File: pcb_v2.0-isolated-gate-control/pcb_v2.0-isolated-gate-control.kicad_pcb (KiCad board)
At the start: 4 copper layers, 170 x 110 mm, 194 parts, among them J1 ServoLock, J10 Buttons, J11 2x encoder, J12 limit-g2, J13 Relay VFD2 [NO, COM, NC], J14 GND-P, J15 OD, J16 Power-LightBarrier-12V, J17 3V3 5V VDD, J18 GNDD, J19 OD, J2 supply, J20 OD, J21 limit-g1, J3 12V 5V, J4 light-barrier, reserve, J5 GND-P, J6 2x remoteControl, J7 Relay VFD1 [NO, COM, NC], J8 RS485, J9 Conn_01x03_Pin, K1 RT314A24, K2 RT314A24, Q1 2N7000, Q2 2N7000, Q3 IRF5305, Q6 IRF5305, U1 ULN2003, U2 esp32-devkit-v1_30Pin, U3 74HC04, U4 MAX485E, U5 L78S05CV_TO220

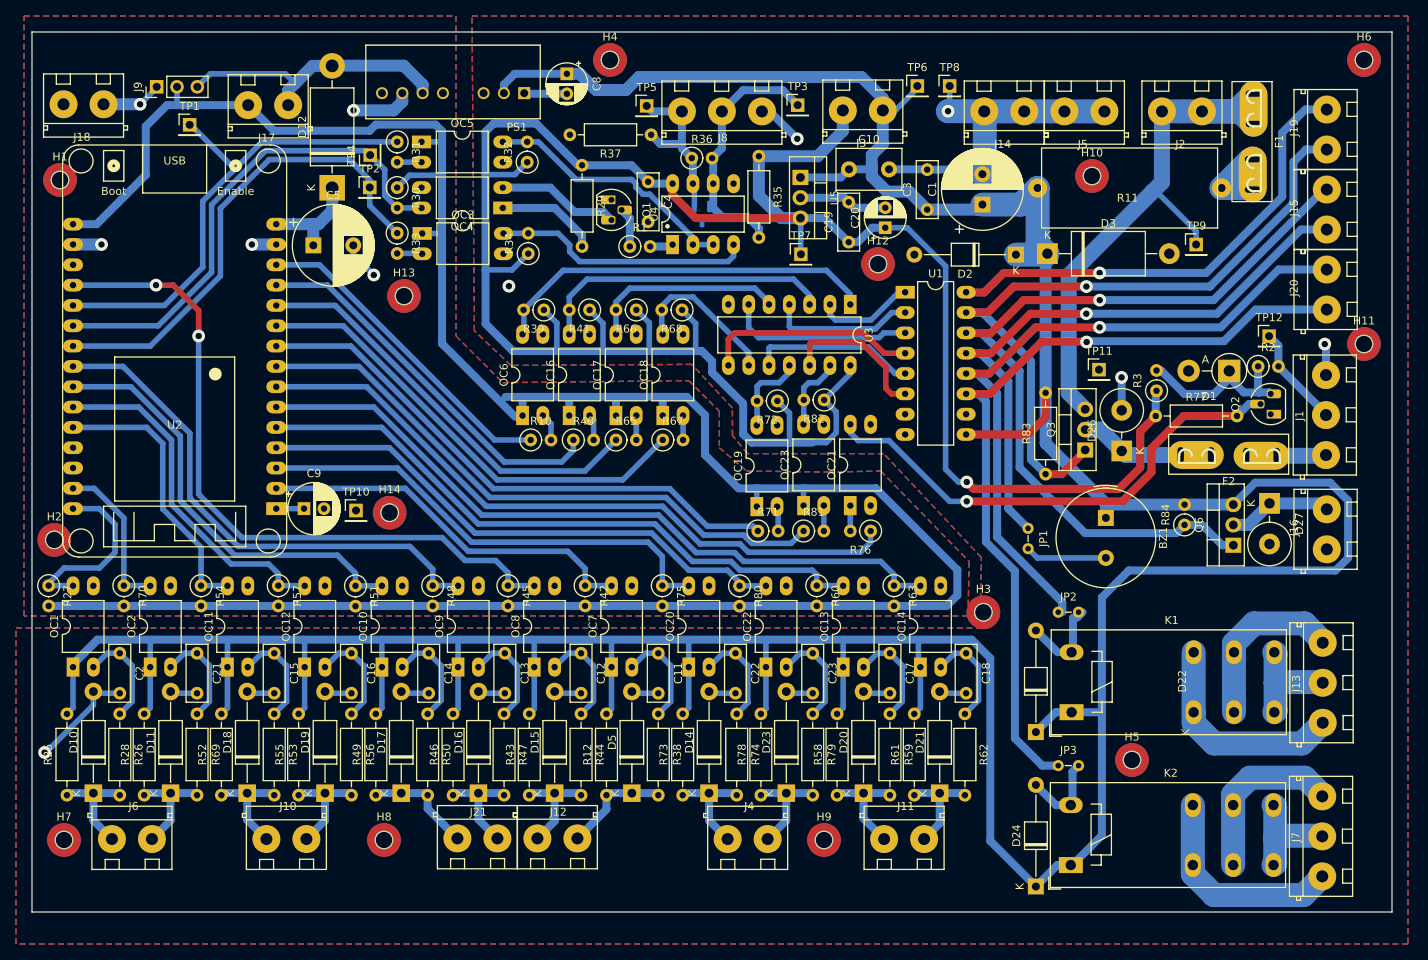
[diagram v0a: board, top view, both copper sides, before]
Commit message: pcb: Invert optocoupler-GPIO connection (high=output on), Layout adjusted (DRC pass)
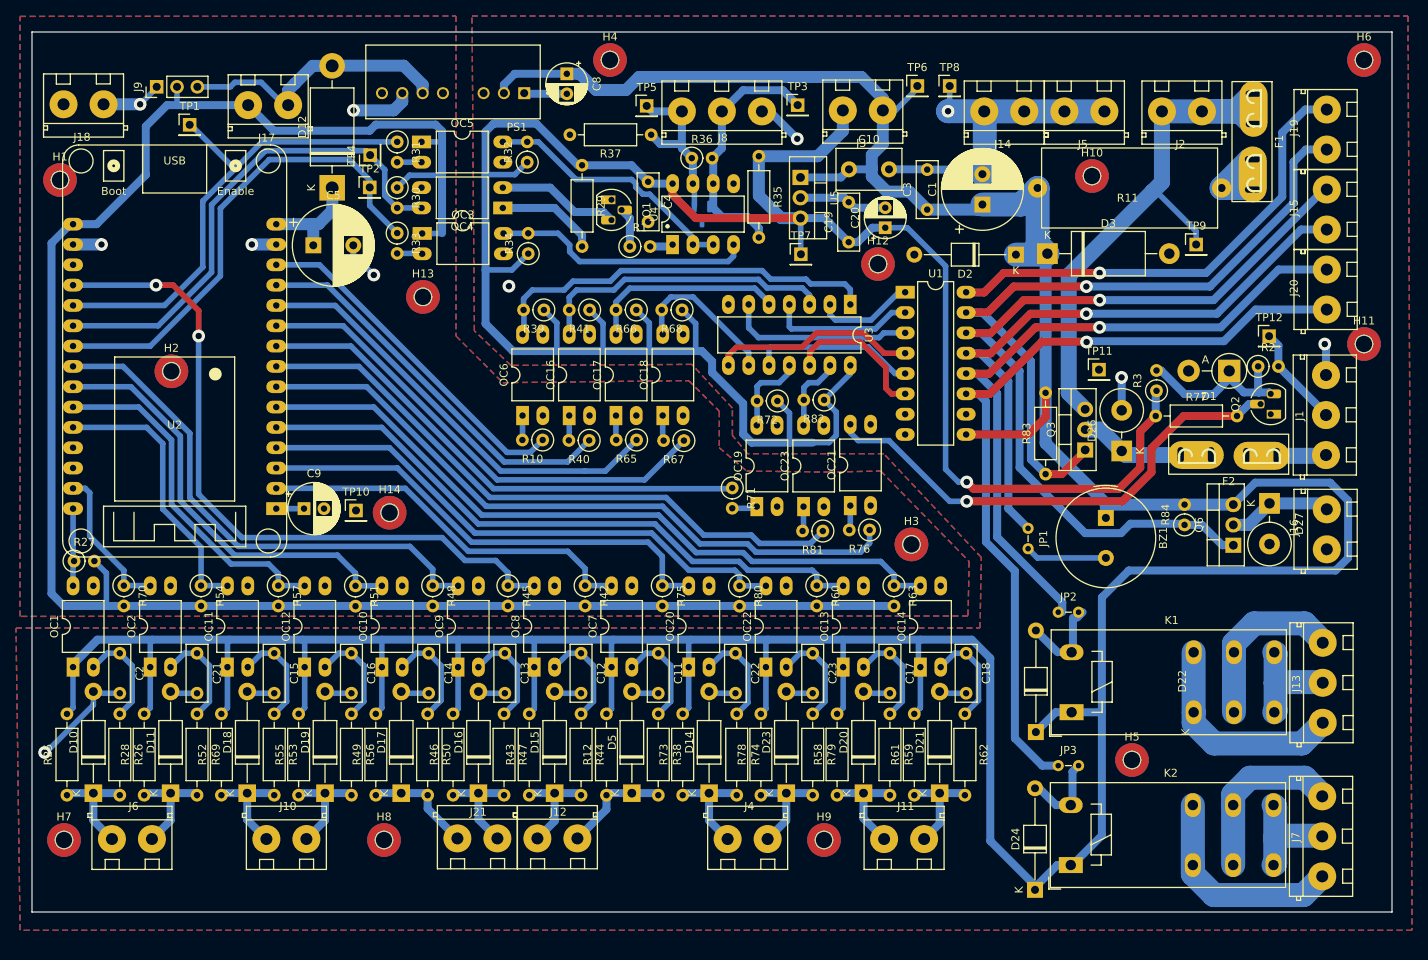
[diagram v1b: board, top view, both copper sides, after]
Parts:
- J4: value light-barrier, reserve -> light-barrier, switch
- R39, R41, R66, R68, R72: value 4k7 -> 6k8
- R82: value 10k -> 6k8
- moved H2 25.7 mm to (52.4, 67.4)
- moved H3 12.4 mm to (144.9, 89.1)
- moved R71 6.26 mm to (122.5, 82.0), turned to -90 degrees
- moved R27 4.41 mm to (40.3, 91.1), turned to 0 degrees
- moved R67 2.65 mm to (116.5, 76.1), turned to 180 degrees
- moved R65 2.57 mm to (110.6, 76.0), turned to 180 degrees
- moved R81 2.41 mm to (133.9, 87.4), turned to 180 degrees
- moved H13 2.37 mm to (83.9, 58.1)
- moved R40 1.98 mm to (104.6, 76.0), turned to 180 degrees
- moved R10 1.50 mm to (98.8, 76.0), turned to 180 degrees
- moved D24 0.43 mm to (160.4, 132.2)
- moved R76 0.18 mm to (139.7, 87.2)
- moved OC23 0.13 mm to (131.4, 84.3)
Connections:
- net /dIn_Reserve renamed /dIn_Switch
- OC16 pad 1: +3V3 -> Net-(OC16-Pad1)
- OC16 pad 2: Net-(OC16-Pad2) -> GND
- OC17 pad 1: +3V3 -> Net-(OC17-Pad1)
- OC17 pad 2: Net-(OC17-Pad2) -> GND
- OC18 pad 1: +3V3 -> Net-(OC18-Pad1)
- OC18 pad 2: Net-(OC18-Pad2) -> GND
- OC19 pad 1: +3V3 -> Net-(OC19-Pad1)
- OC19 pad 2: Net-(OC19-Pad2) -> GND
- OC23 pad 1: +3V3 -> Net-(OC23-Pad1)
- OC23 pad 2: Net-(OC23-Pad2) -> GND
- OC6 pad 1: +3V3 -> Net-(OC6-Pad1)
- OC6 pad 2: Net-(OC6-Pad2) -> GND
- R10 pad 2: Net-(OC6-Pad2) -> Net-(OC6-Pad1)
- R40 pad 2: Net-(OC16-Pad2) -> Net-(OC16-Pad1)
- R65 pad 2: Net-(OC17-Pad2) -> Net-(OC17-Pad1)
- R67 pad 2: Net-(OC18-Pad2) -> Net-(OC18-Pad1)
- R71 pad 2: Net-(OC19-Pad2) -> Net-(OC19-Pad1)
- R81 pad 2: Net-(OC23-Pad2) -> Net-(OC23-Pad1)
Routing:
- net +3V3: track 311.5 -> 244.0 mm
- net /dIn_RemoteOpen: track 22.8 -> 9.79 mm
- net /dOut_RelayEnVFD2: track 69.7 -> 64.4 mm
- net Net-(OC6-Pad2): track 3.47 -> 0.00 mm
- net Net-(OC16-Pad2): track 3.27 -> 0.00 mm
- net Net-(OC23-Pad2): track 3.18 -> 0.00 mm
- net Net-(OC18-Pad1): track 0.00 -> 3.17 mm
- net Net-(OC19-Pad1): track 0.00 -> 3.15 mm
- net Net-(OC16-Pad1): track 0.00 -> 3.12 mm
- net Net-(OC19-Pad2): track 3.11 -> 0.00 mm
- net Net-(OC23-Pad1): track 0.00 -> 3.10 mm
- net Net-(OC17-Pad1): track 0.00 -> 3.07 mm
- net Net-(OC6-Pad1): track 0.00 -> 3.06 mm
- net Net-(OC18-Pad2): track 3.06 -> 0.00 mm
- net Net-(OC17-Pad2): track 3.06 -> 0.00 mm
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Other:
- board text added: "12x digital-in Switch to GND non-inverting"
- board text added: "Gate V2.0 28.12.2024 pcb_isolated-gate-control"
- board text added: "LightBarrier Switch"
- board text added: "pullups to 12V"
- board text removed: "<="
- board text removed: "Digital Inputs"
- board text removed: "LightBarrier RESERVE"
- board text removed: "Switch to GND non-inverting"
- board text removed: "pcb_isolated-gate-control Gate V2.0 28.12.2024"

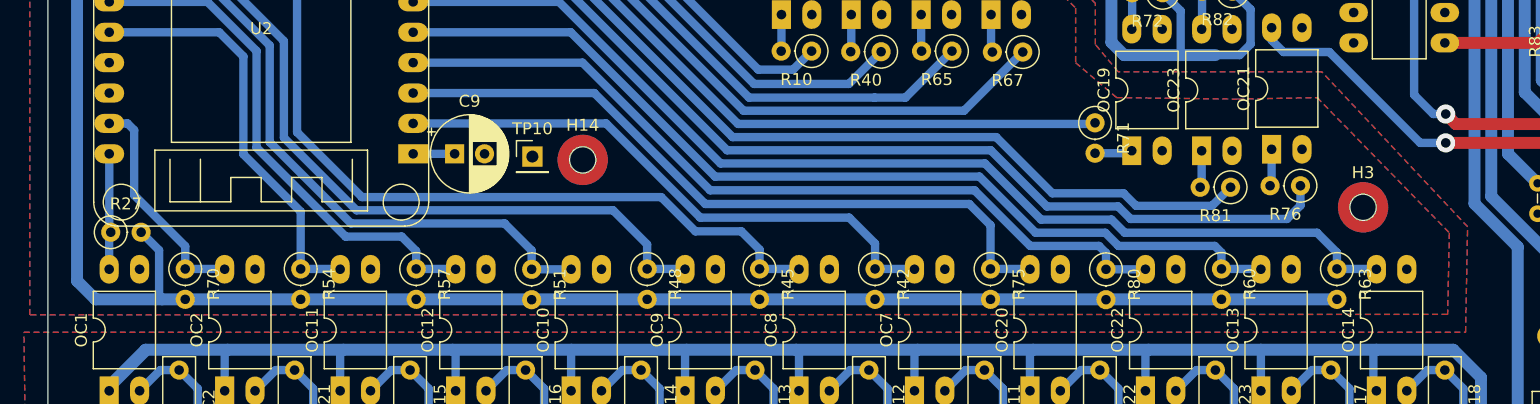
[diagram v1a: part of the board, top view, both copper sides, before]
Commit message: pcb: Cleanup Schematic, arrange, replace legacy-symbols, optimize for ERC pass
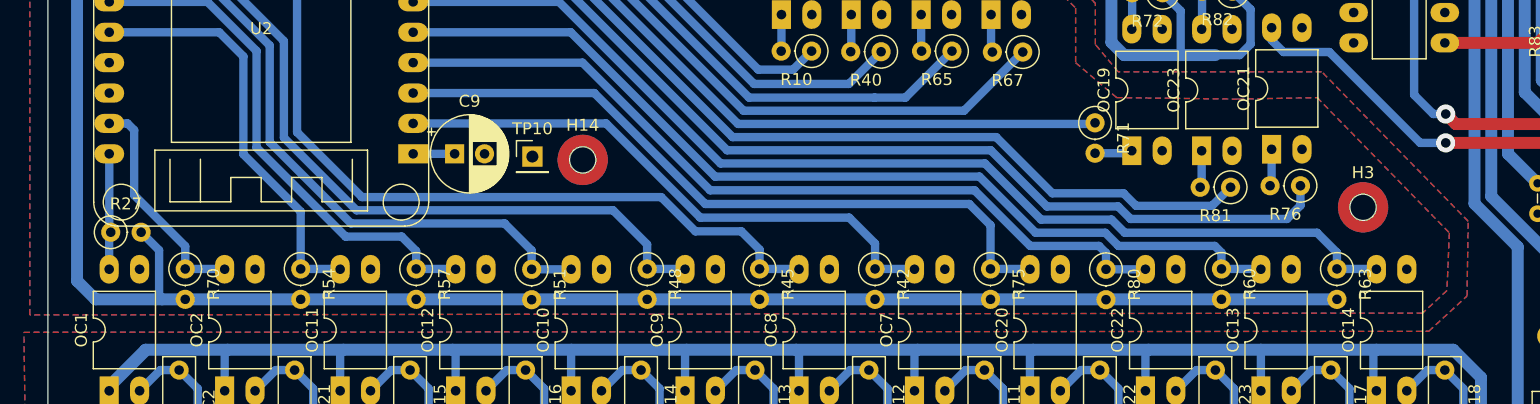
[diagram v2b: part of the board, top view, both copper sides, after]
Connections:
- net RS485_A renamed /RS485-A
- net RS485_B renamed /RS485-B

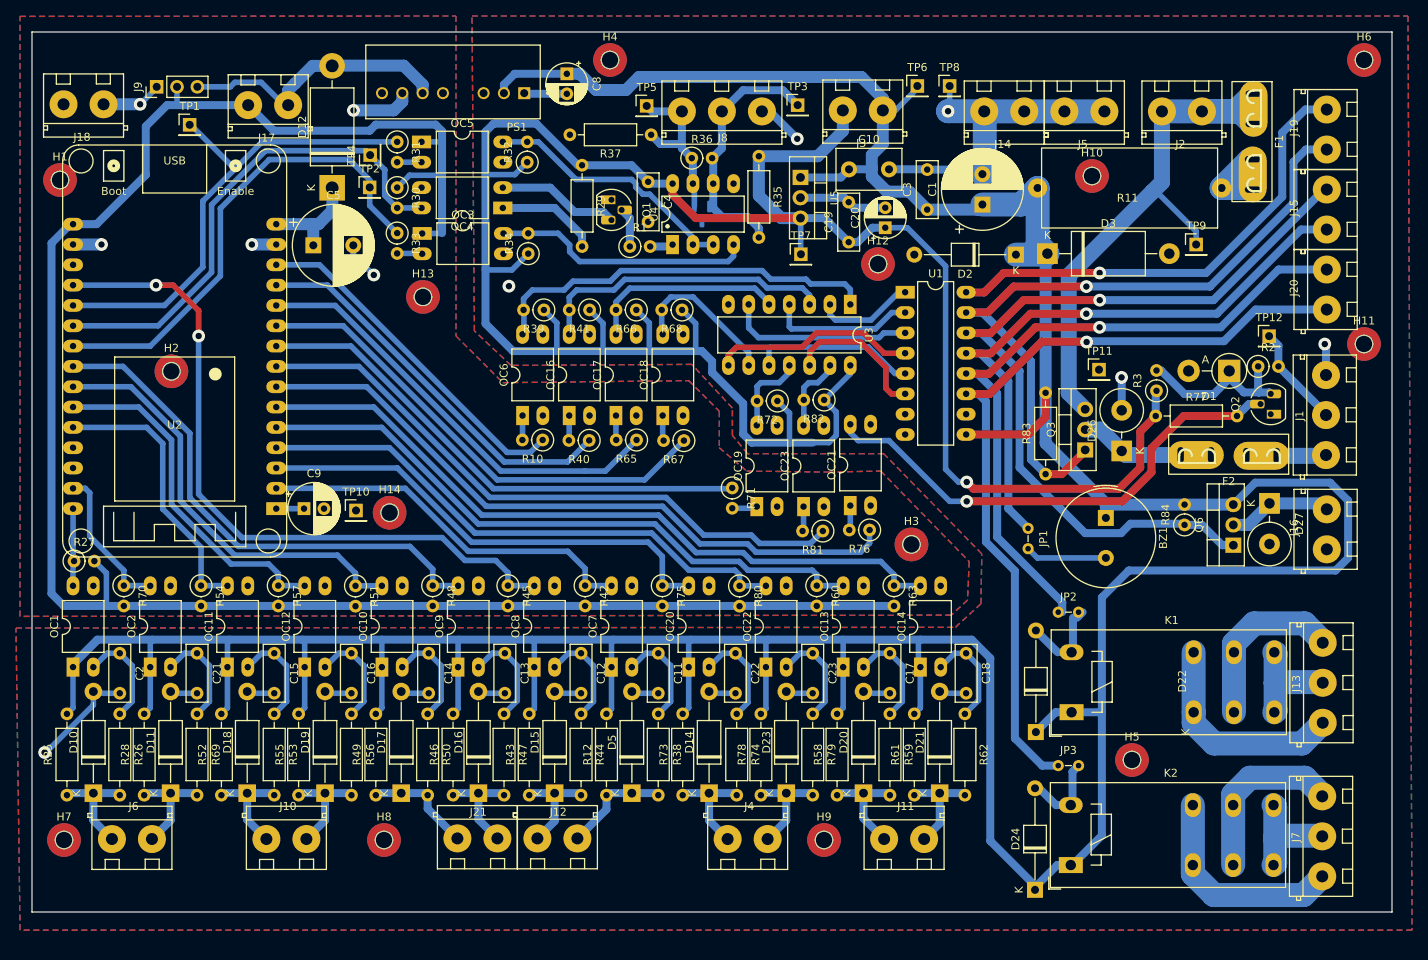
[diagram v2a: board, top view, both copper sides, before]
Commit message: pcb: finish todos, Fix esp32 power issues, document tests, dualType C footprint
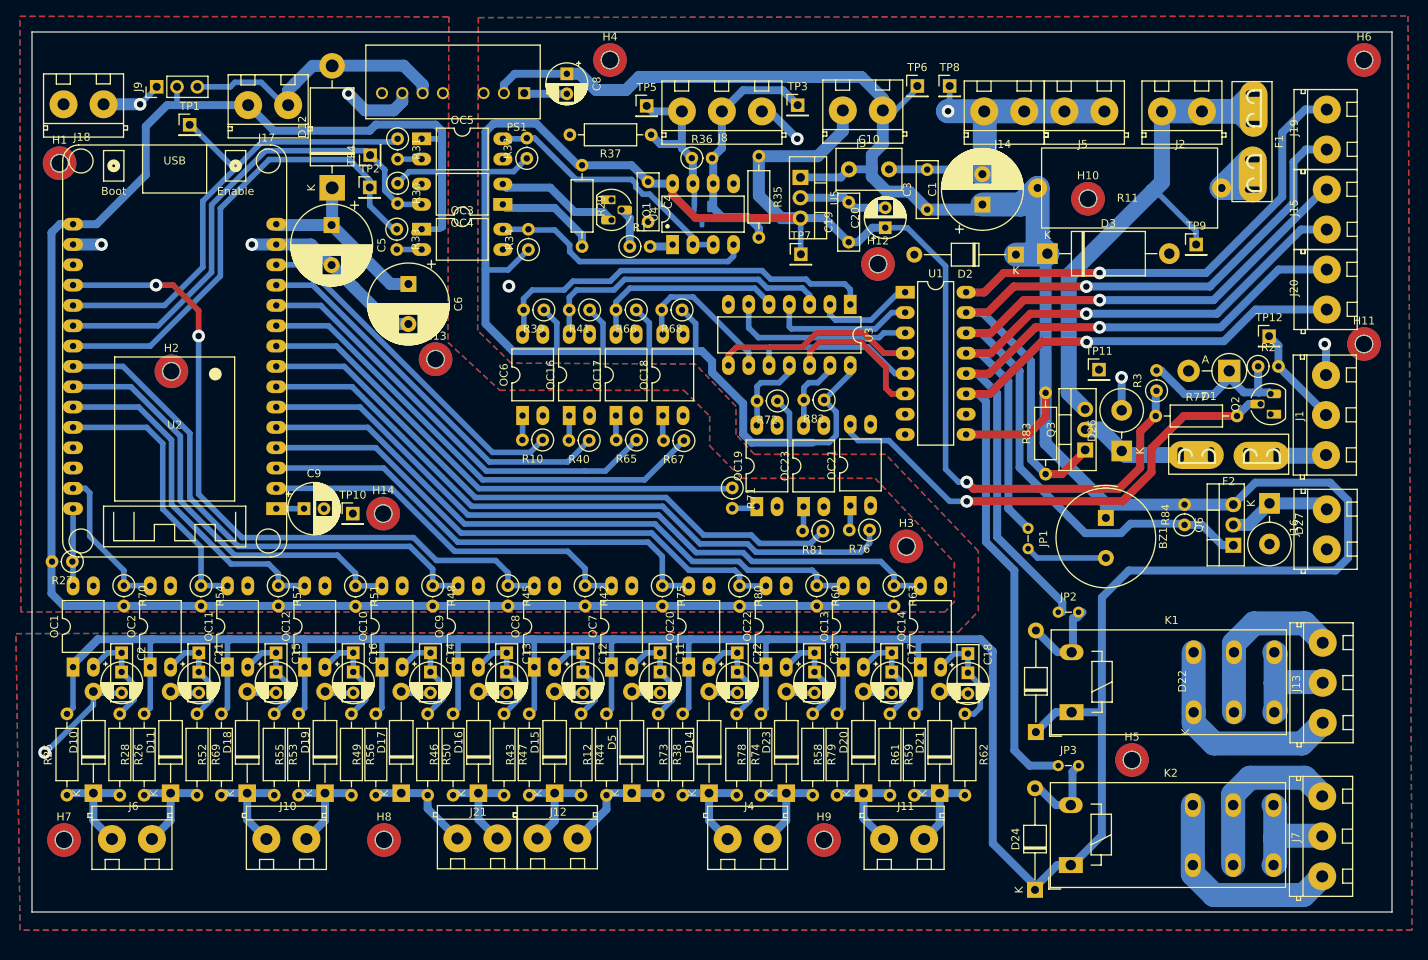
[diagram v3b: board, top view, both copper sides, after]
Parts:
- added C6: 2200uF, Capacitor_THT:CP_Radial_D10.0mm_P5.00mm, F.Cu at (82.0, 56.5)
- C11, C12, C13, C14, C15, C16, C17, C18, C2, C21, C22, C23: footprint Capacitor_THT:C_Disc_D7.0mm_W2.5mm_P5.00mm -> capacitor_libJonny:C_DualType__Disc-7.0x2.5mm-P5mm__Elko-D5mm-P2.5mm
- C5: value 330uF -> 2200uF
- R31, R33: value 470 -> 330
- moved H13 7.94 mm to (85.5, 65.9)
- moved C5 3.41 mm to (72.5, 49.1), turned to -90 degrees
- moved H10 2.89 mm to (167.0, 45.9)
- moved H1 2.10 mm to (38.5, 41.4)
- moved H14 0.81 mm to (78.9, 85.2)
- moved H3 0.68 mm to (144.3, 89.3)
- moved TP10 0.56 mm to (75.1, 85.2)
- moved R30 0.55 mm to (80.7, 43.9)
- moved OC3 0.54 mm to (83.7, 49.6)
- moved R34 0.51 mm to (97.0, 52.2)
- moved R33 0.49 mm to (80.6, 49.6)
- moved R32 0.48 mm to (96.8, 40.8)
- moved OC4 0.45 mm to (93.8, 46.5)
- moved R31 0.39 mm to (80.7, 38.4)
- moved OC5 0.39 mm to (83.7, 38.4)
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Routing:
- net GND: track 26.6 -> 44.0 mm, vias 5 -> 4
- net Net-(D12-K): track 13.2 -> 24.3 mm
- net +3V3: track 244.0 -> 238.1 mm
- net +12V: track 553.3 -> 554.6 mm
- net Net-(J20-Pin_1): track 103.1 -> 104.0 mm
- net Net-(C18-Pad1): track 12.8 -> 13.7 mm
- net /RS485-UART_RX_INVERTED: track 62.4 -> 61.9 mm
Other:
- board text added: "Gate V2.0 31.12.2024 pcb_isolated-gate-control"
- board text removed: "Gate V2.0 28.12.2024 pcb_isolated-gate-control"

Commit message: pcb: Arrange silk/fab text, Mark front-solder, Add schematic+layout export
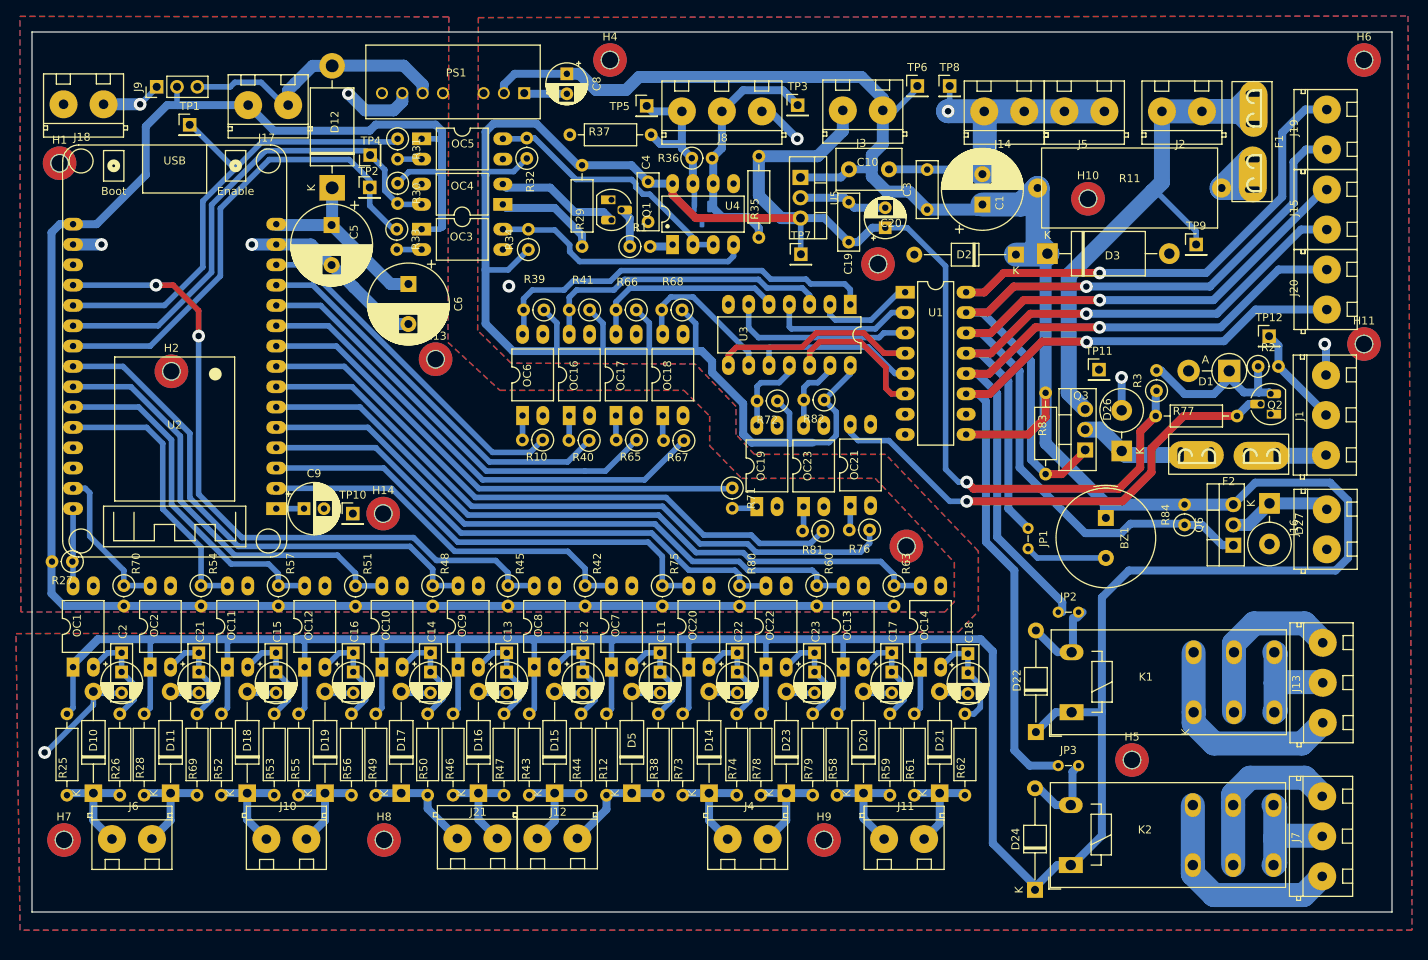
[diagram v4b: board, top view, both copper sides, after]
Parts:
- D10, D11, D14, D15, D16, D17, D18, D19, D20, D21, D23, D5: value TVS 1.5KE30A (starts 28.5V) -> TVS P6KE15A (12.8V)
- D3: value TVS 28V (starts 31V) -> TVS P6KE15A (12.8V)
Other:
- board text added: "Layer User7: Marked pads to solder on top side"
